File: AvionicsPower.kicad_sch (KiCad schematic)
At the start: 59 parts, among them J1 TEST PAD, J2 Conn_01x02, P1 USB_C_Plug, Q1 AO3400A, Q2 AO3400A, Q3 NCE8205, U1 TLV62585RWTR, U2 TPS77533PWPR, U3 RP2040, U4 AP2112K-3.3, U5 W25Q128JVS, U6 Shenzhen Fuman Elec FM2113, U8 MAX98357A, X1 ABM8-272-T3

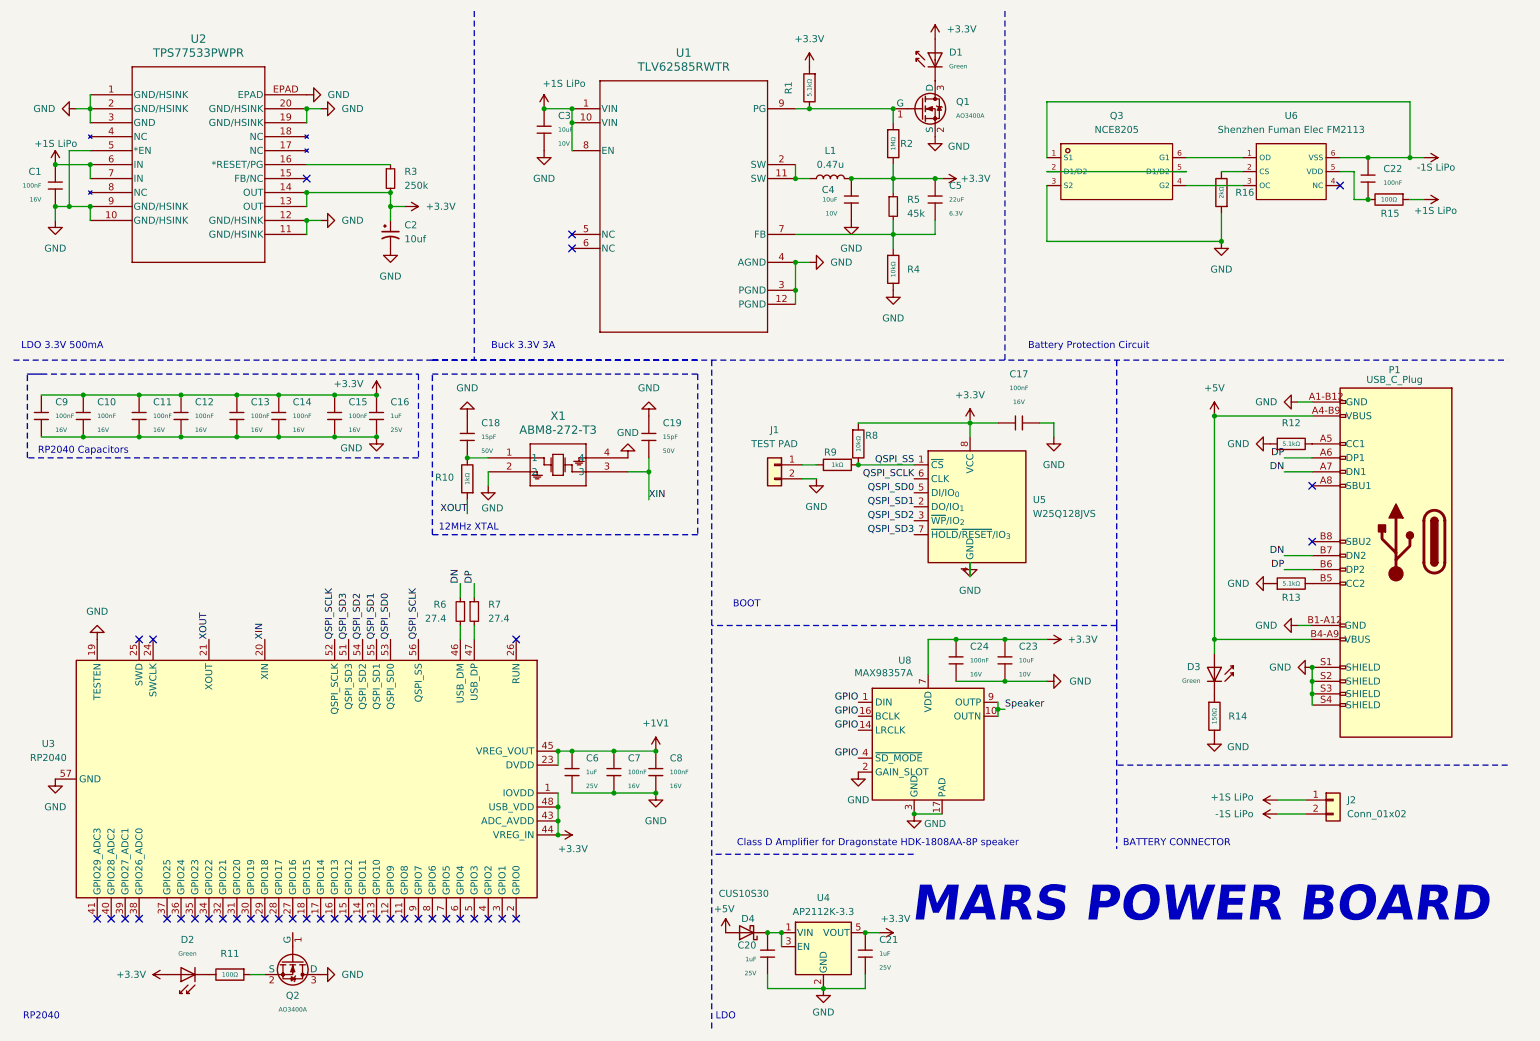
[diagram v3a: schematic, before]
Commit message: Added CAN Controller and Transciever, finalized schematic
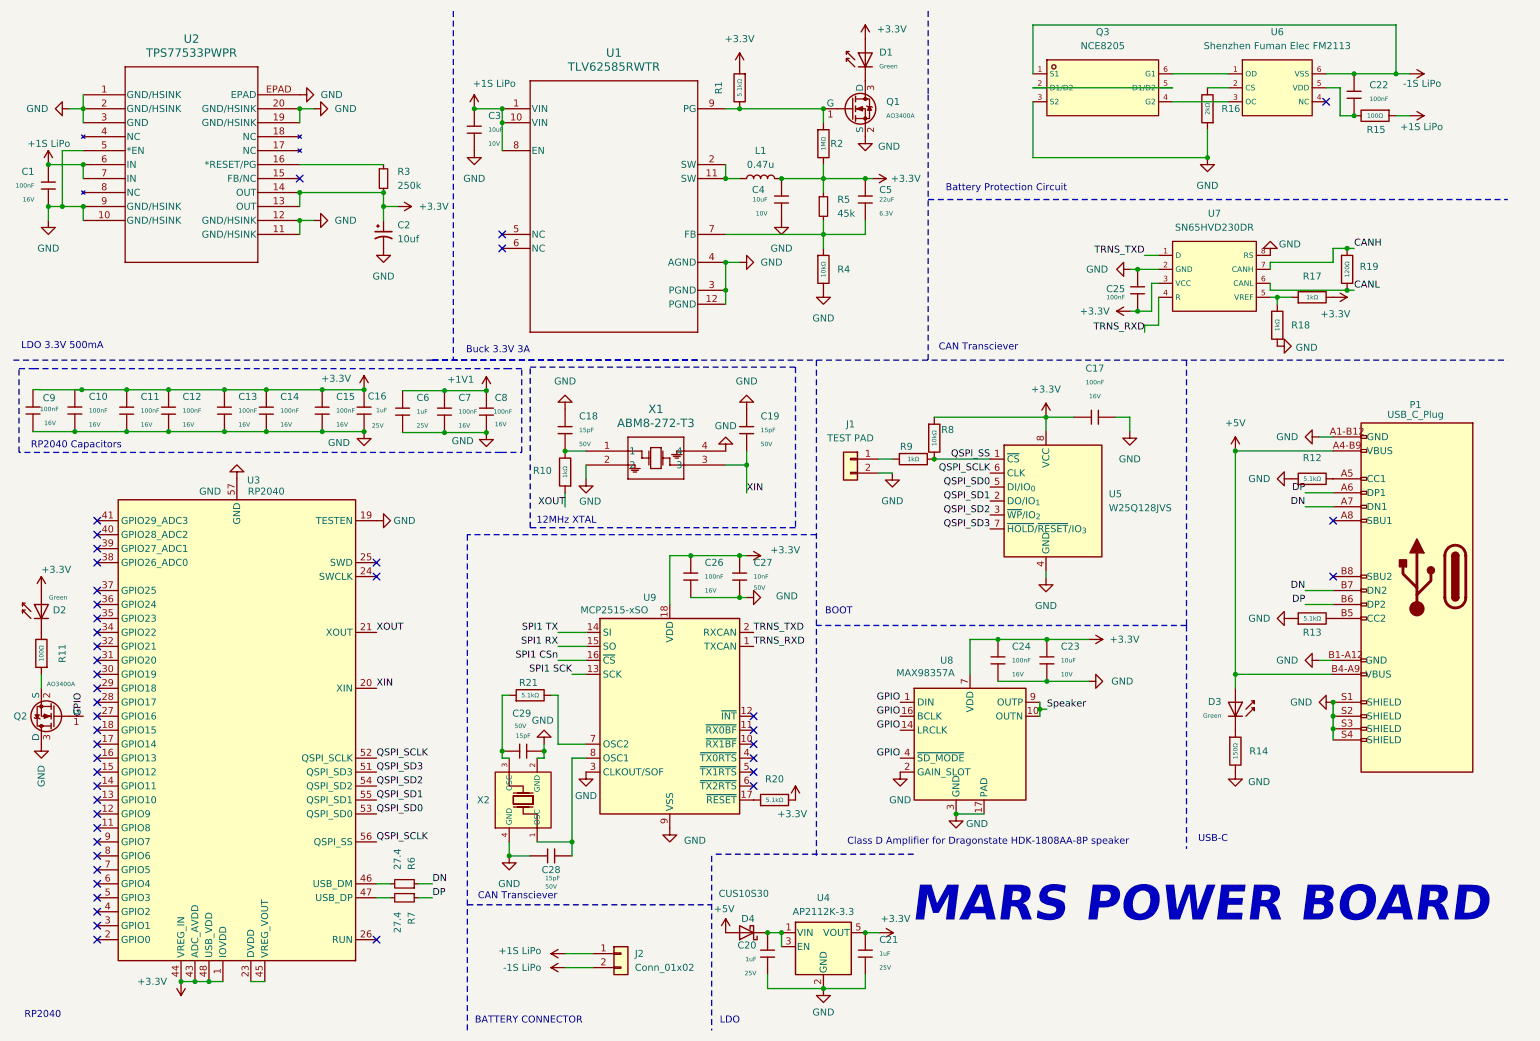
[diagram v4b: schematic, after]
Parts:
- added C25, C26: 100nF, PCM_JLCPCB:C_0402, symbol PCM_JLCPCB-Capacitors:0402,100nF
- added C27: 10nF, PCM_JLCPCB:C_0402, symbol PCM_JLCPCB-Capacitors:0402,10nF
- added C28, C29: 15pF, PCM_JLCPCB:C_0402, symbol PCM_JLCPCB-Capacitors:0402,15pF
- added R17, R18: 1kΩ, PCM_JLCPCB:R_0402, symbol PCM_JLCPCB-Resistors:0402,1kΩ
- added R19: 120Ω, PCM_JLCPCB:R_0402, symbol PCM_JLCPCB-Resistors:0402,120Ω
- added R20, R21: 5.1kΩ, PCM_JLCPCB:R_0402, symbol PCM_JLCPCB-Resistors:0402,5.1kΩ
- added U7: SN65HVD230DR, PCM_JLCPCB:SOIC-8_L4.9-W3.9-P1.27-LS6.0-BL, symbol PCM_JLCPCB-Interface:Transceiver, CAN, SN65HVD230DR
- added U9: MCP2515-xSO, Package_DFN_QFN:QFN-20-1EP_4x4mm_P0.5mm_EP2.5x2.5mm, symbol Interface_CAN_LIN:MCP2515-xSO
- added X2: X322512MSB4SI, PCM_JLCPCB:CRYSTAL-SMD_4P-L3.2-W2.5-BL, symbol PCM_JLCPCB-Crystals:Crystal, 12MHz, 20pF
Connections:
- net +1V1: no longer U3.23 (DVDD), U3.45 (VREG_VOUT), U3.50 (DVDD)
- net +3.3V: now also C25.2, C26.1, C27.1, R17.2, R20.2, U7.3 (VCC), U9.18 (VDD)
- net GND: now also C25.1, C26.2, C27.2, C28.1, C29.1, R18.1, U7.2 (GND), U7.8 (RS), U9.3 (CLKOUT/SOF), U9.9 (VSS), X2.2 (GND), X2.4 (GND)
- net GPIO: now also Q2.1 (G)
- new net: C29.2, R21.1, X2.3 (OSC)
- new net: C28.2, U9.8 (OSC1), X2.1 (OSC)
- new net: R17.1, R18.2, U7.5 (VREF)
- new net: U3.23 (DVDD), U3.45 (VREG_VOUT), U3.50 (DVDD)
- new net: R20.1, U9.17 (~{RESET})
- new net: R21.2, U9.7 (OSC2)
- new net CANH: R19.1, U7.7 (CANH)
- new net CANL: R19.2, U7.6 (CANL)
- new net SPI1 CSn: U9.16 (~{CS})
- new net SPI1 RX: U9.15 (SO)
- new net SPI1 SCK: U9.13 (SCK)
- new net SPI1 TX: U9.14 (SI)
- new net TRNS_RXD: U7.4 (R), U9.1 (TXCAN)
- new net TRNS_TXD: U7.1 (D), U9.2 (RXCAN)
- no-connect marks 39 -> 45
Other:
- note added: "CAN Transciever"
- note added: "USB-C"
- moved on the sheet: C1, C10, C11, C12, C13, C14, C15, C16, C17, C18, C19, C2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

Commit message: Began PCB Layout
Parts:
- added J3: Conn_01x03_Pin, symbol Connector:Conn_01x03_Pin
- added R22: 1kΩ, Resistor_SMD:R_0402_1005Metric, symbol PCM_JLCPCB-Resistors:0402,1kΩ
- J2: footprint (none) -> Connector_AMASS:AMASS_XT60PW-M_1x02_P7.20mm_Horizontal
- P1: footprint (none) -> Connector_USB:USB_C_Receptacle_GCT_USB4105-xx-A_16P_TopMnt_Horizontal
- R1, R10, R11, R12, R13, R15, R16, R17, R18, R19, R20, R21, R8, R9: footprint PCM_JLCPCB:R_0402 -> Resistor_SMD:R_0402_1005Metric
- R2: footprint PCM_JLCPCB:R_0603 -> Resistor_SMD:R_0603_1608Metric
- X1: footprint ABM8-272-T3_ABR -> Crystal:Crystal_SMD_3225-4Pin_3.2x2.5mm
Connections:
- net +1V1: now also U3.23 (DVDD), U3.45 (VREG_VOUT), U3.50 (DVDD)
- net +3.3V: now also J3.3 (Pin_3), R22.2
- net QSPI_SCLK: no longer U3.56 (QSPI_SS)
- net QSPI_SD1: no longer U5.2 (DO/IO_{1})
- net SPI1 CSn: now also U3.56 (QSPI_SS), R22.1
- net SWCLK: now reaches U3.24 (SWCLK)
- net SWCLK: now also J3.2 (Pin_2)
- net SWD: now reaches U3.25 (SWD)
- net SWD: now also J3.1 (Pin_1)
- net QSPI_SD0 renamed QSPI_SDI
- net QSPI_SDI: no longer U3.53 (QSPI_SD0)
- new net QSPI_SDO: U3.53 (QSPI_SD0), U5.2 (DO/IO_{1})
- no-connect marks 45 -> 43
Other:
- moved on the sheet: C18, C19, R10, X1

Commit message: basic layout
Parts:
- removed R14: 150Ω, PCM_JLCPCB:R_0805, symbol PCM_JLCPCB-Resistors:0805,150Ω
- added R23: 200Ω, PCM_JLCPCB:R_0402, symbol PCM_JLCPCB-Resistors:0402,200Ω
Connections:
- net +1S LiPo: now also J2.2 (Pin_2); no longer J2.1 (Pin_1)
- net -1S LiPo: now also J2.1 (Pin_1); no longer J2.2 (Pin_2)
- net GND: now also R23.2
- net at D3.1: now also R23.1

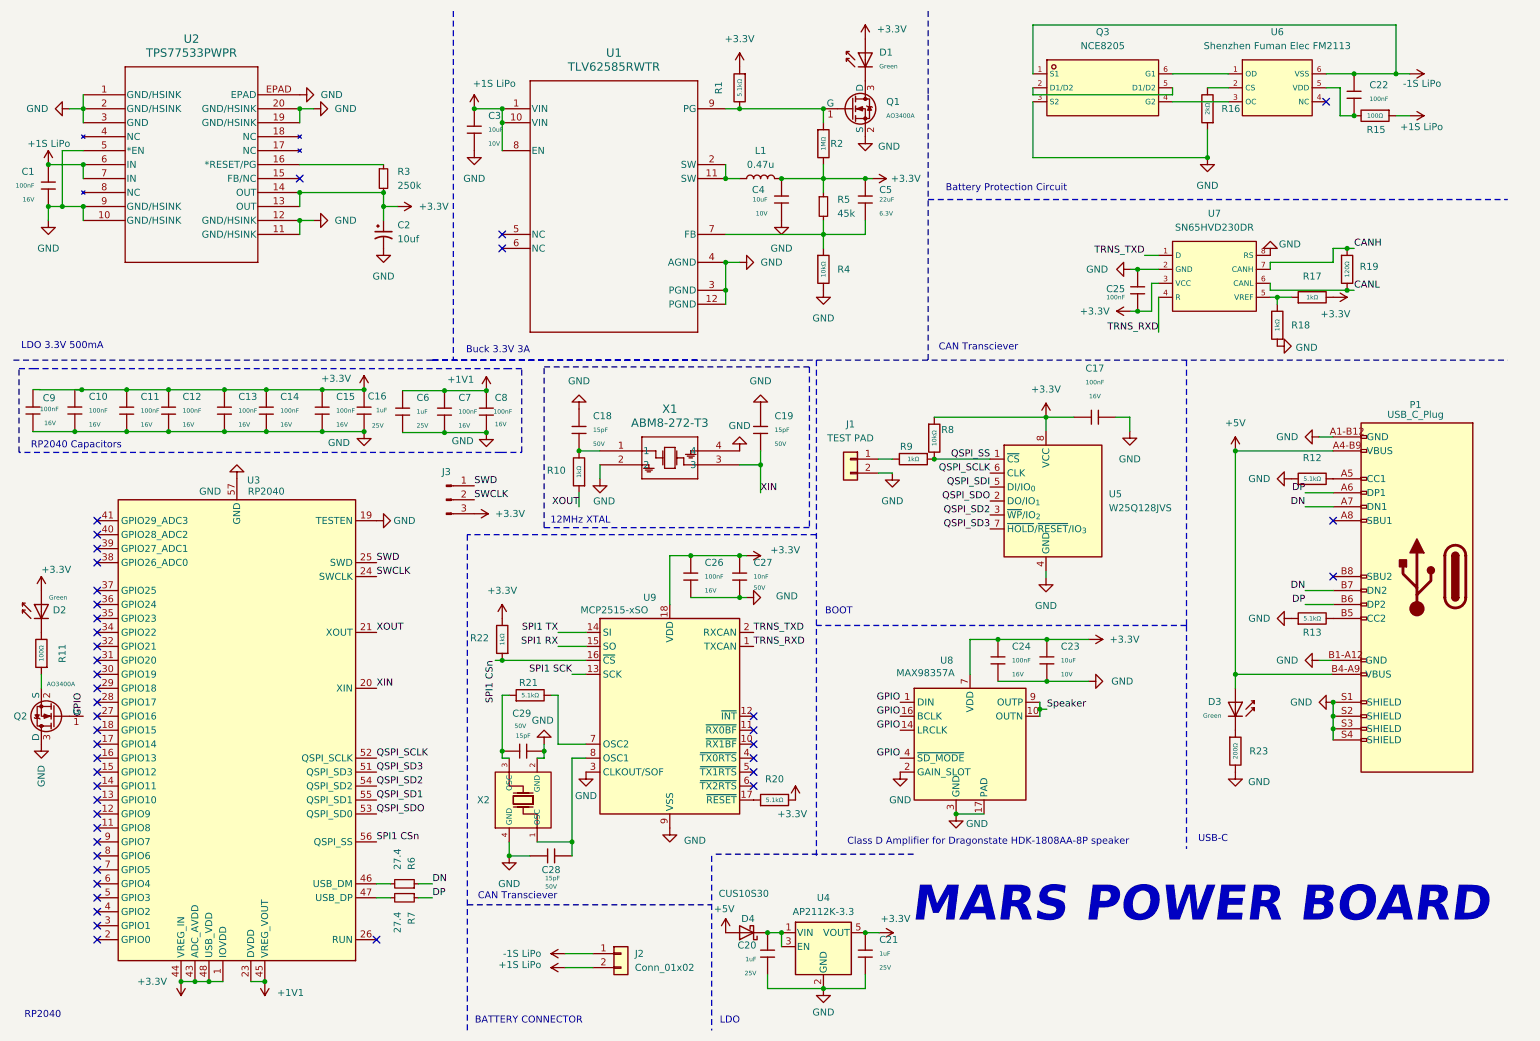
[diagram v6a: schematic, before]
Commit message: Finalized PCB layout.
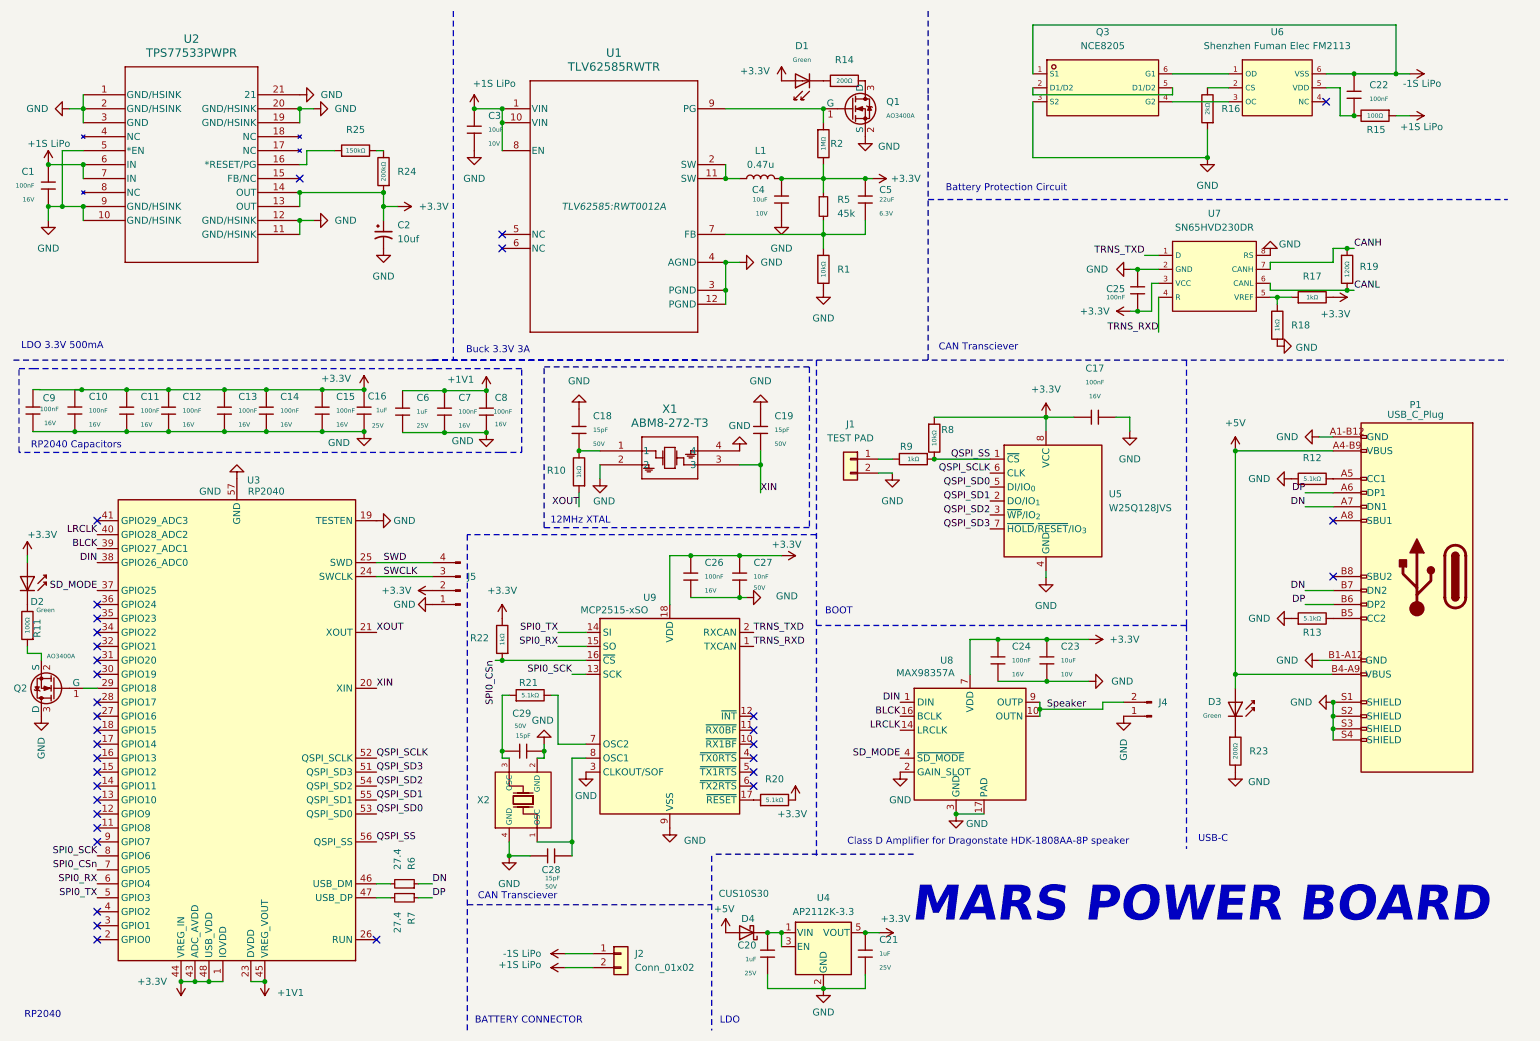
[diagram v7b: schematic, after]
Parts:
- removed J3: Conn_01x03_Pin, symbol Connector:Conn_01x03_Pin
- removed R1: 5.1kΩ, Resistor_SMD:R_0402_1005Metric, symbol PCM_JLCPCB-Resistors:0402,5.1kΩ
- removed R3: 250k, PCM_JLCPCB:R_1206, symbol Device:R_Small
- removed R4: 10kΩ, PCM_JLCPCB:R_0805, symbol PCM_JLCPCB-Resistors:0805,10kΩ
- added J4: Conn_01x02_Pin, Connector_JST:JST_PH_B2B-PH-K_1x02_P2.00mm_Vertical, symbol Connector:Conn_01x02_Pin
- added J5: Conn_01x04_Pin, Connector_PinHeader_2.00mm:PinHeader_1x04_P2.00mm_Vertical, symbol Connector:Conn_01x04_Pin
- added R1: 10kΩ, PCM_JLCPCB:R_0402, symbol PCM_JLCPCB-Resistors:0402,10kΩ
- added R14: 200Ω, PCM_JLCPCB:R_0402, symbol PCM_JLCPCB-Resistors:0402,200Ω
- added R24: 200kΩ, PCM_JLCPCB:R_0402, symbol PCM_JLCPCB-Resistors:0402,200kΩ
- added R25: 150kΩ, PCM_JLCPCB:R_0402, symbol PCM_JLCPCB-Resistors:0402,150kΩ
- J1: footprint (none) -> TestPoint:TestPoint_Pad_1.0x1.0mm
- L1: footprint (none) -> PCM_JLCPCB:L_0805
- R5: footprint (none) -> PCM_JLCPCB:C_0402; LCSC (none) -> C334700
- U1: footprint RWT0012A -> TLV62585:RWT0012A
- U2: footprint PWP20_3P38X2P4 -> TPS77533:PWP20_3P38X2P4; LCSC (none) -> C406872
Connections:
- net SPI1 RX is gone; now on net SPI0_RX: U9.15 (SO)
- net SPI1 SCK is gone; now on net SPI0_SCK: U9.13 (SCK)
- net SPI1 TX is gone; now on net SPI0_TX: U9.14 (SI)
- net +3.3V: now also J5.2 (Pin_2), R24.1
- net GND: now also U2.21, J4.1 (Pin_1), J5.1 (Pin_1), R1.2; no longer U2.EPAD
- net QSPI_SD1: now also U5.2 (DO/IO_{1})
- net QSPI_SS: now also U3.56 (QSPI_SS)
- net SWCLK: now also J5.3 (Pin_3)
- net SWD: now also J5.4 (Pin_4)
- net Speaker: now also J4.2 (Pin_2)
- net at U2.16 (*RESET/PG): now also R25.1
- net at C5.2, R5.2, U1.7 (FB): now also R1.1
- net at U3.29 (GPIO18): now also Q2.1 (G)
- net SD_MODE: now reaches U3.37 (GPIO25)
- net SD_MODE: now also U8.4 (~{SD_MODE})
- net DIN: now reaches U3.38 (GPIO26_ADC0)
- net DIN: now also U8.1 (DIN)
- net BLCK: now reaches U3.39 (GPIO27_ADC1)
- net BLCK: now also U8.16 (BCLK)
- net LRCLK: now reaches U3.40 (GPIO28_ADC2)
- net LRCLK: now also U8.14 (LRCLK)
- net SPI0_TX: now reaches U3.5 (GPIO3)
- net SPI0_RX: now reaches U3.6 (GPIO4)
- net SPI0_CSn: now reaches U3.7 (GPIO5)
- net SPI0_CSn: now also R22.1, U9.16 (~{CS})
- net SPI0_SCK: now reaches U3.8 (GPIO6)
- net at D1.1: now also R14.1; no longer Q1.3 (D)
- removed net GPIO: Q2.1 (G), U8.1 (DIN), U8.14 (LRCLK), U8.16 (BCLK), U8.4 (~{SD_MODE})
- net QSPI_SDI renamed QSPI_SD0
- net QSPI_SD0: now also U3.53 (QSPI_SD0)
- removed net QSPI_SDO: U3.53 (QSPI_SD0), U5.2 (DO/IO_{1})
- removed net SPI1 CSn: R22.1, U3.56 (QSPI_SS), U9.16 (~{CS})
- new net: R24.2, R25.2
- new net: Q1.3 (D), R14.2
- no-connect marks 43 -> 34
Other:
- moved on the sheet: D1, D2, Q2, R11

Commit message: Changed connector, passed DRC, finalized PCB design
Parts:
- J2: footprint Connector_AMASS:AMASS_XT60PW-M_1x02_P7.20mm_Horizontal -> Connector_JST:JST_PH_B2B-PH-K_1x02_P2.00mm_Vertical
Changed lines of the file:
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@@
 			)
 		)
-		(property "Footprint" "Connector_AMASS:AMASS_XT60PW-M_1x02_P7.20mm_Horizontal"
+		(property "Footprint" "Connector_JST:JST_PH_B2B-PH-K_1x02_P2.00mm_Vertical"
 			(at 123.19 184.15 0)
 			(effects
